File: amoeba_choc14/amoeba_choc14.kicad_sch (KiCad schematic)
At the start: 6 parts, among them J1 Conn_01x01_Pin, J2 Conn_01x01_Pin, J3 Conn_01x01_Pin, J4 Conn_01x01_Pin, SW1 SW_SPST

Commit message: feat(PCBA): add LCSC number for diode
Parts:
- D1: LCSC (none) -> C81598
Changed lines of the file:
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@@
+			)
+		)
+		(property "LCSC" "C81598"
+			(at 144.78 106.68 0)
+			(effects
+				(font
+					(size 1.27 1.27)
+				)
+				(hide yes)
 			)
 		)

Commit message: feat: extrude from BOM and position file
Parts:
- J1, J2, J3, J4: now left out of the parts list
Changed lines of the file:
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@@
 		(unit 1)
 		(exclude_from_sim no)
-		(in_bom yes)
+		(in_bom no)
 		(on_board yes)
 		(dnp no)
@@
 		(unit 1)
 		(exclude_from_sim no)
-		(in_bom yes)
+		(in_bom no)
 		(on_board yes)
 		(dnp no)
@@
 		(unit 1)
 		(exclude_from_sim no)
-		(in_bom yes)
+		(in_bom no)
 		(on_board yes)
 		(dnp no)
@@
 		(unit 1)
 		(exclude_from_sim no)
-		(in_bom yes)
-		(on_board yes)
-		(dnp no)
+		(in_bom no)
+		(on_board yes)
+		(dnp no)

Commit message: feat: Config "do not fit"
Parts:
- J1, J2, J3, J4, SW1: Config (none) -> do not fit
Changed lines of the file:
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@@
+			)
+		)
+		(property "Config" "do not fit"
+			(at 133.35 116.84 0)
+			(effects
+				(font
+					(size 1.27 1.27)
+				)
+				(hide yes)
 			)
 		)
@@
 			)
 		)
+		(property "Config" "do not fit"
+			(at 129.54 95.25 0)
+			(effects
+				(font
+					(size 1.27 1.27)
+				)
+				(hide yes)
+			)
+		)
 		(pin "1"
 		)
@@
 			)
 		)
+		(property "Config" "do not fit"
+			(at 134.62 106.68 0)
+			(effects
+				(font
+					(size 1.27 1.27)
+				)
+				(hide yes)
+			)
+		)
 		(pin "1"
 		)
@@
 			)
 		)
+		(property "Config" ""
+			(at 144.78 106.68 0)
+			(effects
+				(font
+					(size 1.27 1.27)
+				)
+				(hide yes)
+			)
+		)
 		(pin "1"
 		)
@@
 		)
 		(property "Description" ""
+			(at 158.75 116.84 0)
+			(effects
+				(font
+					(size 1.27 1.27)
+				)
+				(hide yes)
+			)
+		)
+		(property "Config" "do not fit"
 			(at 158.75 116.84 0)
 			(effects
@@
 			(at 129.54 121.92 0)
 			(effects
+				(font
+					(size 1.27 1.27)
+				)
+				(hide yes)
+			)
+		)
+		(property "Config" "do not fit"
+			(at 129.54 121.92 0)
+			(effects

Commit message: feat(schematic): exclude switch from BOM
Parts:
- SW1: now left out of the parts list
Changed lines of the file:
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@@
 		(unit 1)
 		(exclude_from_sim no)
-		(in_bom yes)
+		(in_bom no)
 		(on_board yes)
 		(dnp no)

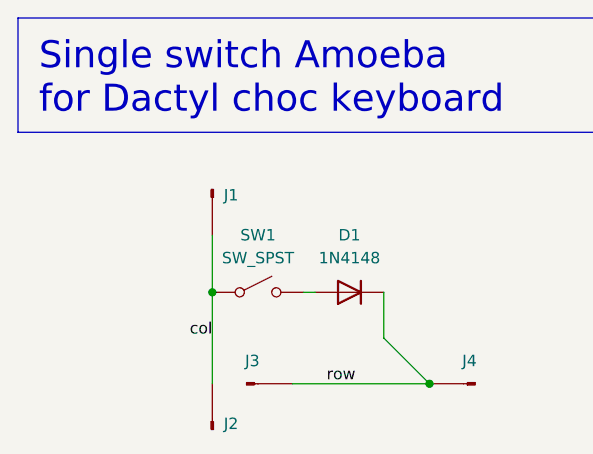
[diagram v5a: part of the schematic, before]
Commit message: feat(amoeba): extra column pad for MCU connection
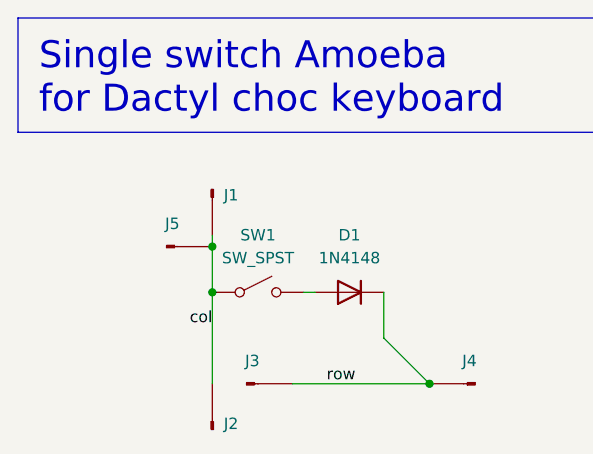
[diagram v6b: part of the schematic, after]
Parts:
- added J5: Conn_01x01_Pin, Amoeba_Choc_Nar:Pin_D0.8mm_L7.0mm, symbol Connector:Conn_01x01_Pin
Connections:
- net col: now also J5.1 (Pin_1)
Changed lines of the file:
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@@
 	(paper "USLetter")
+	(junction
+		(at 129.54 101.6)
+		(diameter 0)
+		(color 0 0 0 0)
+	)
 	(junction
 		(at 129.54 106.68)
@@
 	(wire
 		(pts
+			(xy 129.54 100.33) (xy 129.54 101.6)
+		)
+		(stroke
+			(width 0)
+			(type default)
+		)
+	)
+	(wire
+		(pts
+			(xy 139.7 106.68) (xy 140.97 106.68)
+		)
+		(stroke
+			(width 0)
+			(type default)
+		)
+	)
+	(wire
+		(pts
 			(xy 129.54 106.68) (xy 129.54 116.84)
 		)
@@
 	(wire
 		(pts
-			(xy 129.54 100.33) (xy 129.54 106.68)
-		)
-		(stroke
-			(width 0)
-			(type default)
-		)
-	)
-	(wire
-		(pts
-			(xy 139.7 106.68) (xy 140.97 106.68)
+			(xy 129.54 101.6) (xy 129.54 106.68)
 		)
 		(stroke
@@
 	)
 	(label "col"
-		(at 129.54 111.76 180)
+		(at 129.54 110.49 180)
 		(fields_autoplaced yes)
 		(effects
@@
 					(unit 1)
 				)
+			)
+		)
+	)
+	(symbol
+		(lib_name "Conn_01x01_Pin_1")
+		(lib_id "Connector:Conn_01x01_Pin")
+		(at 124.46 101.6 0)
+		(unit 1)
+		(exclude_from_sim no)
+		(in_bom no)
+		(on_board yes)
+		(dnp no)
+		(fields_autoplaced yes)
+		(property "Reference" "J5"
+			(at 125.095 99.06 0)
+			(effects
+				(font
+					(size 1.27 1.27)
+				)
+			)
+		)
+		(property "Value" "Conn_01x01_Pin"
+			(at 126.365 100.33 90)
+			(effects
+				(font
+					(size 1.27 1.27)
+				)
+				(justify left)
+				(hide yes)
+			)
+		)
+		(property "Footprint" "Amoeba_Choc_Nar:Pin_D0.8mm_L7.0mm"
+			(at 124.46 101.6 0)
+			(effects
+				(font
+					(size 1.27 1.27)
+				)
+				(hide yes)
+			)
+		)
+		(property "Datasheet" "~"
+			(at 124.46 101.6 0)
+			(effects
+				(font
+					(size 1.27 1.27)
+				)
+				(hide yes)
+			)
+		)
+		(property "Description" ""
+			(at 124.46 101.6 0)
+			(effects
+				(font
+					(size 1.27 1.27)
+				)
+				(hide yes)
+			)
+		)
+		(property "Config" "do not fit"
+			(at 124.46 101.6 0)
+			(effects
+				(font
+					(size 1.27 1.27)
+				)
+				(hide yes)
+			)
+		)
+		(pin "1"
+		)
+		(instances
+			(project "amoeba_choc14"
+				(path "/c1f16e18-f6ca-463c-9cde-8f3fe4c41e25"
+					(reference "J5")
+					(unit 1)
+				)

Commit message: feat(sch): Title block info
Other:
- title: (none) -> Amoeba Choc 14
- moved on the sheet: D1, J1, J2, J3, J4, J5, SW1

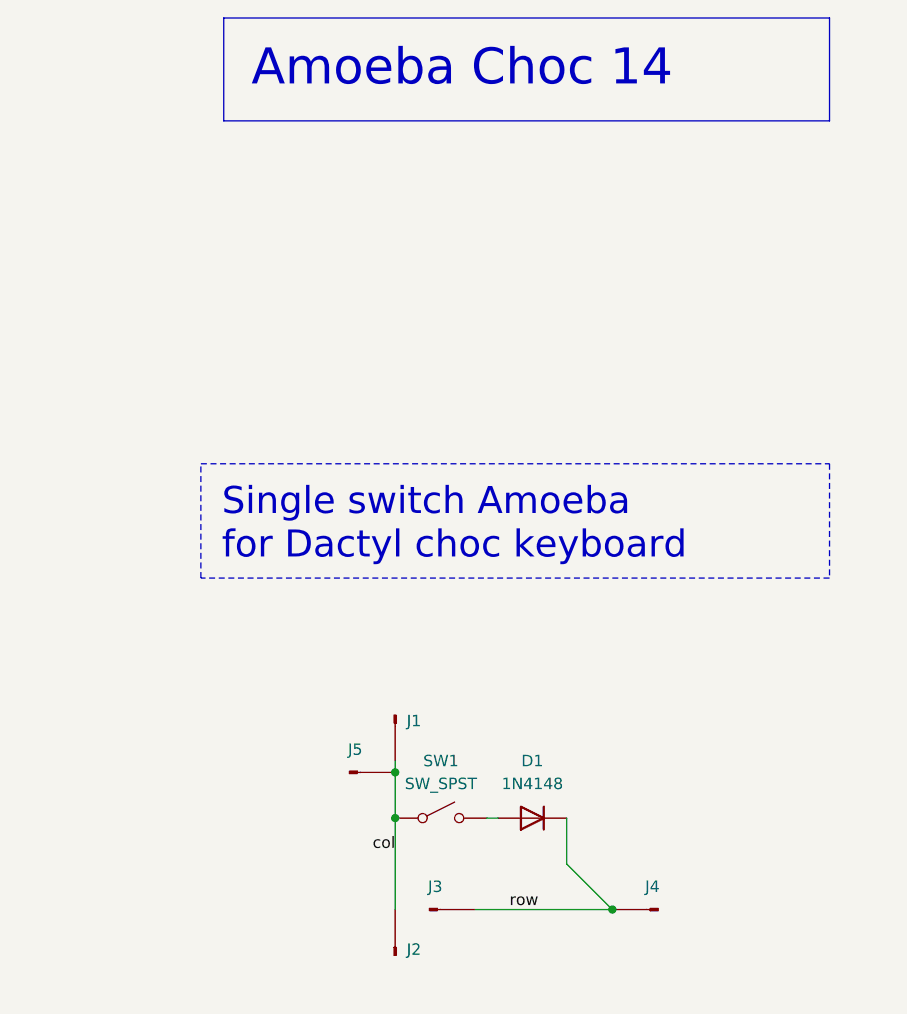
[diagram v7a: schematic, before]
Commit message: feat: width 13.7 mm, clearer row/col silk
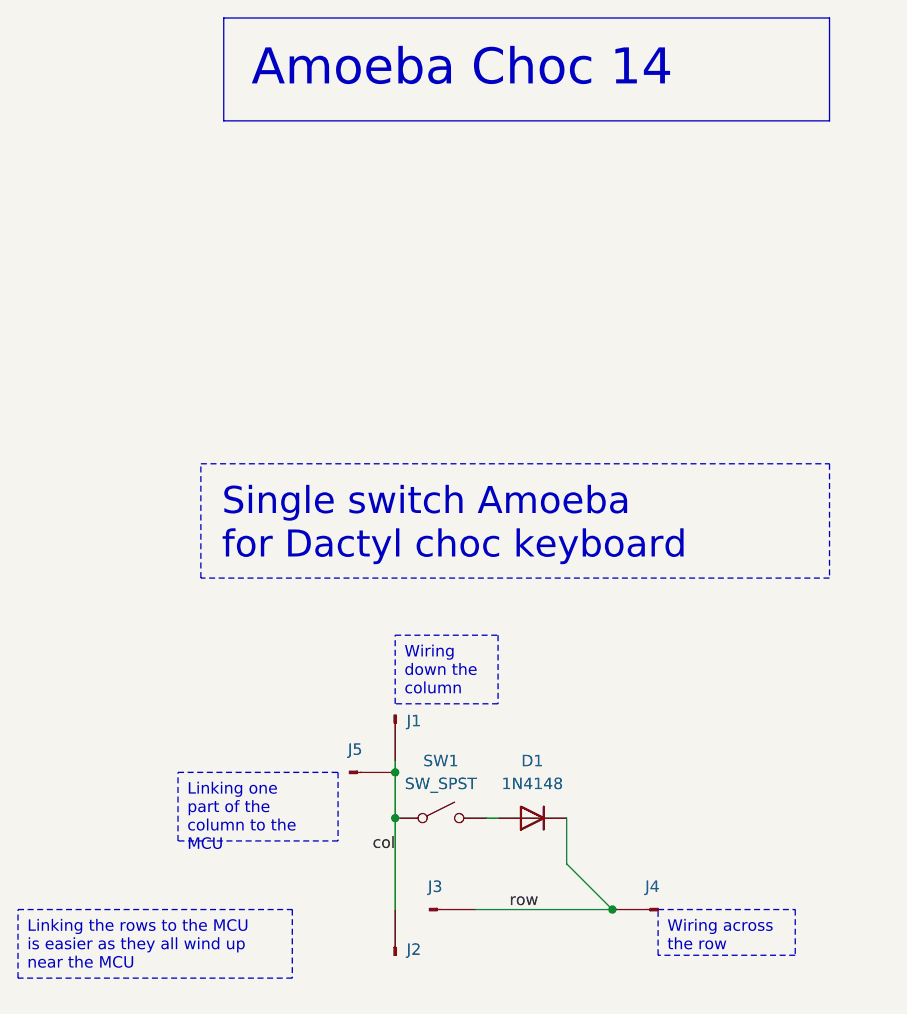
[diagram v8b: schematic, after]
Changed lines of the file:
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@@
+		)
+	)
+	(text_box "Linking one part of the column to the MCU"
+		(exclude_from_sim no)
+		(at 100.33 97.79 0)
+		(size 17.78 7.62)
+		(stroke
+			(width 0)
+			(type dot)
+		)
+		(fill
+			(type none)
+		)
+		(effects
+			(font
+				(size 1.27 1.27)
+			)
+			(justify left top)
+		)
+	)
+	(text_box "Linking the rows to the MCU\nis easier as they all wind up near the MCU"
+		(exclude_from_sim no)
+		(at 82.55 113.03 0)
+		(size 30.48 7.62)
+		(stroke
+			(width 0)
+			(type dot)
+		)
+		(fill
+			(type none)
+		)
+		(effects
+			(font
+				(size 1.27 1.27)
+			)
+			(justify left top)
 		)
 	)
@@
 			)
 			(justify left top)
+		)
+	)
+	(text_box "Wiring down the column"
+		(exclude_from_sim no)
+		(at 124.46 82.55 0)
+		(size 11.43 7.62)
+		(stroke
+			(width 0)
+			(type dot)
+		)
+		(fill
+			(type none)
+		)
+		(effects
+			(font
+				(size 1.27 1.27)
+			)
+			(justify left top)
+		)
+	)
+	(text_box "Wiring across the row"
+		(exclude_from_sim no)
+		(at 153.67 113.03 0)
+		(size 15.24 5.08)
+		(stroke
+			(width 0)
+			(type dot)
+		)
+		(fill
+			(type none)
+		)
+		(effects
+			(font
+				(size 1.27 1.27)
+			)
+			(justify left top)
